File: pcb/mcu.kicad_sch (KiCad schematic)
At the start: 15 parts, among them J301 Conn_02x05_Top_Bottom, J302 1658525-9, U301 EFM32GG990F1024, Y301 Crystal_GND24

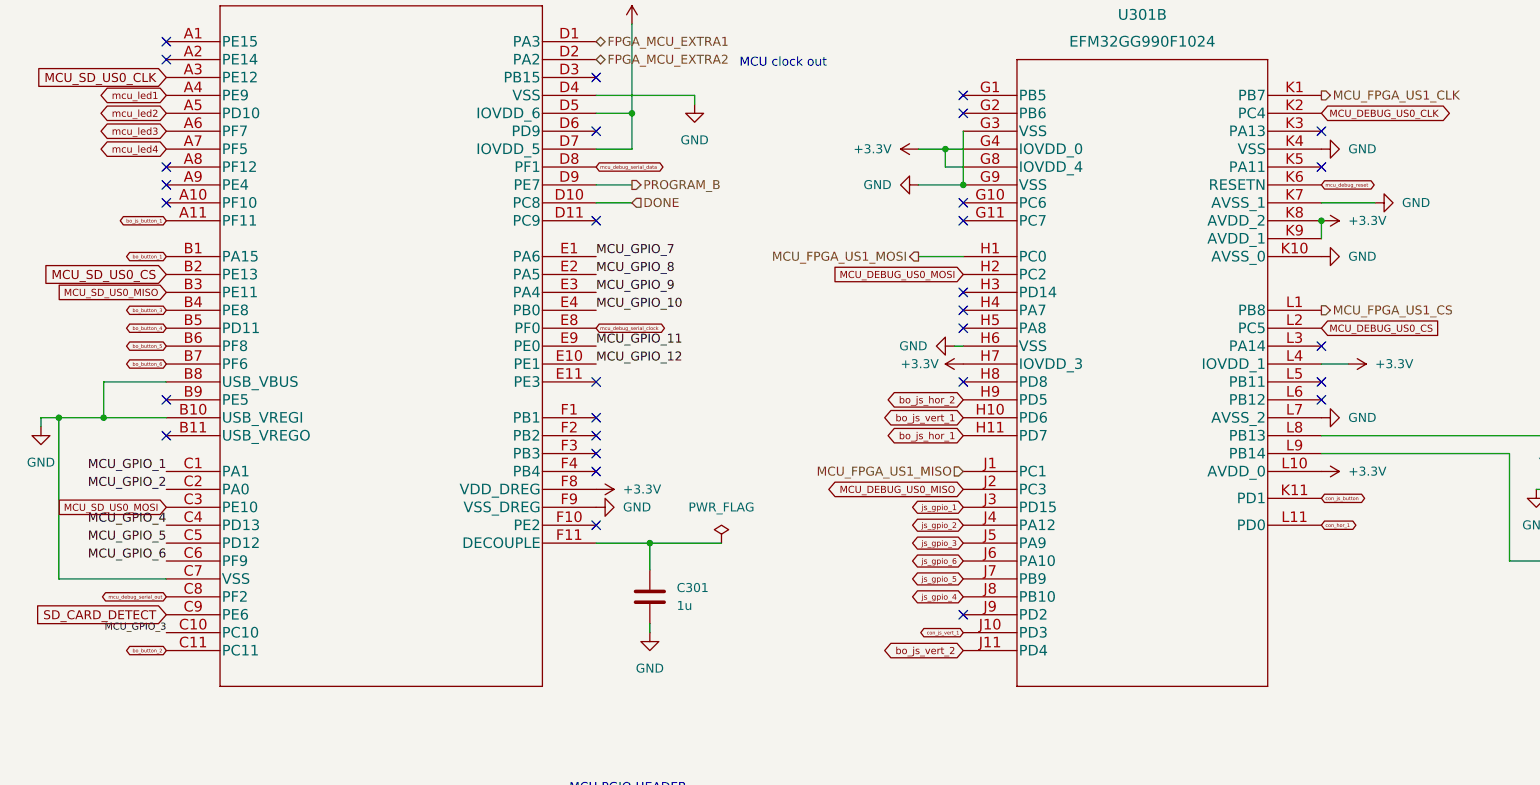
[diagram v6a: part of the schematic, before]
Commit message: switch some pins for more erqonomiq layout
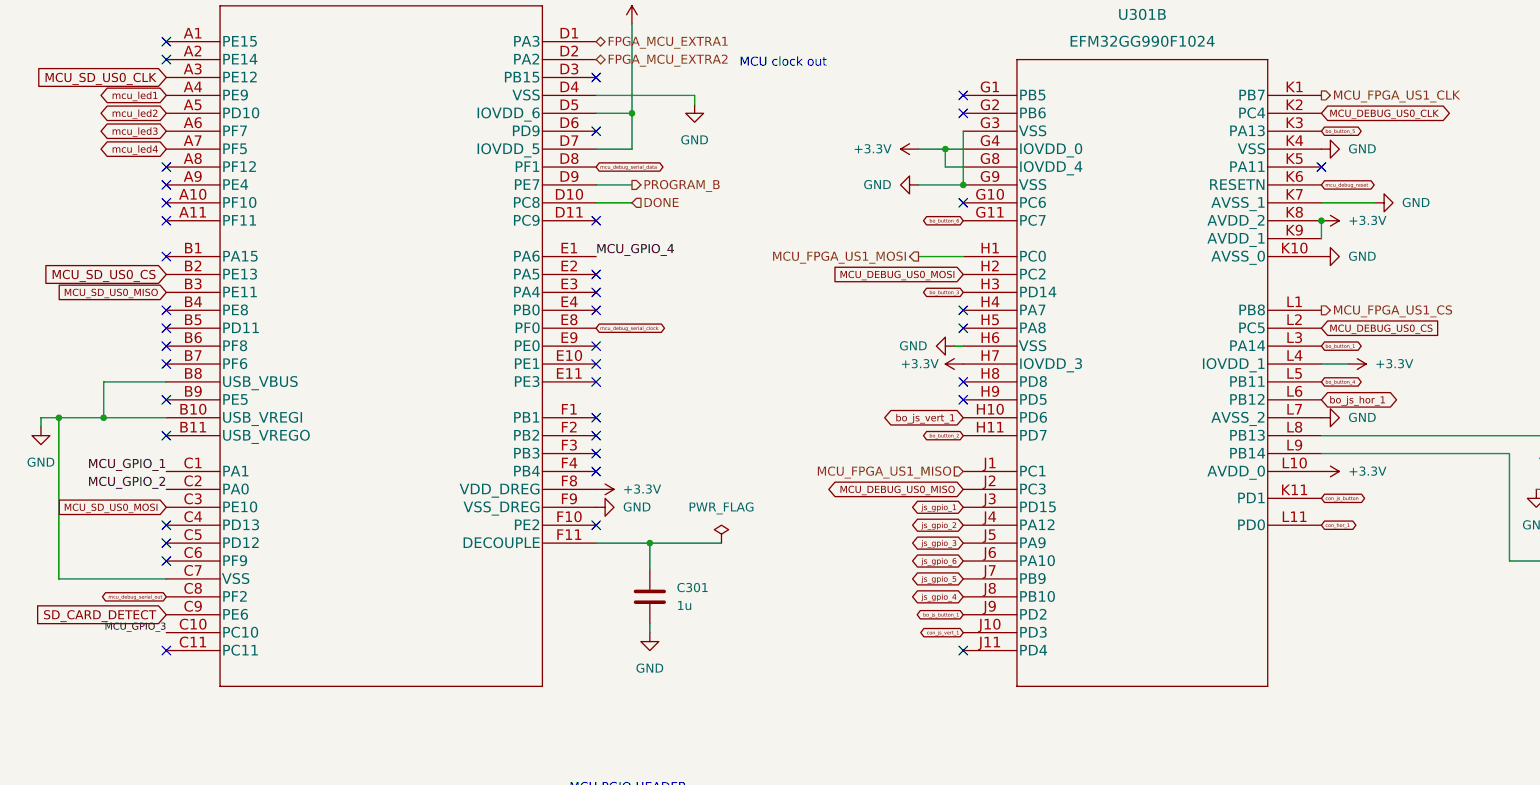
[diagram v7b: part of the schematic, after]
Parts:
- U301: footprint BGA112 -> mcu_kicad:EFM32GG990F1024
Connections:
- net MCU_GPIO_7 is gone; now on net MCU_GPIO_4: U301.E1 (PA6)
- net MCU_GPIO_4: no longer U301.C4 (PD13)
- net bo_button_1: now also U301.L3 (PA14); no longer U301.B1 (PA15)
- net bo_button_2: now also U301.H11 (PD7); no longer U301.C11 (PC11)
- net bo_button_3: now also U301.H3 (PD14); no longer U301.B4 (PE8)
- net bo_button_4: now also U301.L5 (PB11); no longer U301.B5 (PD11)
- net bo_button_5: now also U301.K3 (PA13); no longer U301.B6 (PF8)
- net bo_button_6: now also U301.G11 (PC7); no longer U301.B7 (PF6)
- net bo_js_button_1: now also U301.J9 (PD2); no longer U301.A11 (PF11)
- net bo_js_hor_1: now also U301.L6 (PB12); no longer U301.H11 (PD7)
- net MCU_GPIO_10: no longer names the net of U301.E4 (PB0)
- net MCU_GPIO_11: no longer names the net of U301.E9 (PE0)
- net MCU_GPIO_12: no longer names the net of U301.E10 (PE1)
- net MCU_GPIO_5: no longer names the net of U301.C5 (PD12)
- net MCU_GPIO_6: no longer names the net of U301.C6 (PF9)
- net MCU_GPIO_8: no longer names the net of U301.E2 (PA5)
- net MCU_GPIO_9: no longer names the net of U301.E3 (PA4)
- net bo_js_hor_2: no longer names the net of U301.H9 (PD5)
- net bo_js_vert_2: no longer names the net of U301.J11 (PD4)
- no-connect marks 39 -> 49

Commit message: workon
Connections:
- net bo_button_3: now also U301.H4 (PA7); no longer U301.H3 (PD14)
- net js_gpio_5: now also U301.H3 (PD14); no longer U301.J7 (PB9)
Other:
- note added: "mcu spi til debug bruker usart 2 location 0"
- note added: "mcu spi til fpga bruker usart 1 location 0"
- note added: "mcu til sd spi bruker usart 0 location 0"
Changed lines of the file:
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@@
   (no_connect (at 95.25 62.23))
   (no_connect (at 34.29 74.93))
-  (no_connect (at 147.32 67.31))
   (no_connect (at 147.32 69.85))
   (no_connect (at 95.25 72.39))
@@
   (no_connect (at 34.29 59.69))
   (no_connect (at 95.25 64.77))
+  (no_connect (at 147.32 105.41))
   (no_connect (at 34.29 67.31))
   (no_connect (at 34.29 72.39))
@@
     (stroke (width 0) (type default) (color 0 0 0 0))
   )
+  (text "mcu til sd spi bruker usart 0 location 0\n" (at -29.21 63.5 0)
+    (effects (font (size 1.27 1.27)) (justify left bottom))
+  )
   (text "MCU PGIO HEADER" (at 91.44 135.89 0)
+    (effects (font (size 1.27 1.27)) (justify left bottom))
+  )
+  (text "mcu spi til debug bruker usart 2 location 0" (at 189.23 20.32 0)
     (effects (font (size 1.27 1.27)) (justify left bottom))
   )
@@
   )
   (text "MCU clock out" (at 115.57 33.02 0)
+    (effects (font (size 1.27 1.27)) (justify left bottom))
+  )
+  (text "mcu spi til fpga bruker usart 1 location 0" (at 124.46 16.51 0)
     (effects (font (size 1.27 1.27)) (justify left bottom))
   )
@@
     )
   )
-  (global_label "bo_button_3" (shape bidirectional) (at 147.32 64.77 180) (fields_autoplaced)
-    (effects (font (size 0.5 0.5)) (justify right))
-    (property "Intersheet References" "${INTERSHEET_REFS}" (id 0) (at 141.8462 64.7388 0)
-      (effects (font (size 0.5 0.5)) (justify right) hide)
-    )
-  )
   (global_label "bo_js_button_1" (shape bidirectional) (at 147.32 110.49 180) (fields_autoplaced)
     (effects (font (size 0.5 0.5)) (justify right))
@@
     )
   )
+  (global_label "js_gpio_5" (shape bidirectional) (at 147.32 64.77 180) (fields_autoplaced)
+    (effects (font (size 0.8 0.8)) (justify right))
+    (property "Intersheet References" "${INTERSHEET_REFS}" (id 0) (at 140.2381 64.72 0)
+      (effects (font (size 0.8 0.8)) (justify right) hide)
+    )
+  )
   (global_label "MCU_DEBUG_US0_MOSI" (shape input) (at 121.92 148.59 0) (fields_autoplaced)
     (effects (font (size 1 1)) (justify left))
@@
     )
   )
+  (global_label "bo_button_3" (shape bidirectional) (at 147.32 67.31 180) (fields_autoplaced)
+    (effects (font (size 0.5 0.5)) (justify right))
+    (property "Intersheet References" "${INTERSHEET_REFS}" (id 0) (at 141.8462 67.2788 0)
+      (effects (font (size 0.5 0.5)) (justify right) hide)
+    )
+  )
   (global_label "mcu_led4" (shape bidirectional) (at 34.29 44.45 180) (fields_autoplaced)
     (effects (font (size 1 1)) (justify right))
@@
     )
   )
-  (global_label "js_gpio_5" (shape bidirectional) (at 147.32 105.41 180) (fields_autoplaced)
-    (effects (font (size 0.8 0.8)) (justify right))
-    (property "Intersheet References" "${INTERSHEET_REFS}" (id 0) (at 140.2381 105.36 0)
-      (effects (font (size 0.8 0.8)) (justify right) hide)
-    )
-  )
